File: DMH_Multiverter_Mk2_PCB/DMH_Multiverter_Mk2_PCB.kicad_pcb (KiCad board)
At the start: 2 copper layers, 32 x 75 mm, 24 parts, among them J0 Conn_01x01, J100 IDC_02x05, J200 BackBone_Connector_6pin, J50 Conn_01x06, J60 Conn_01x06, U1 TL072

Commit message: Main PCB update ongoing
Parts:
- added R6: 1k, Resistor_THT:R_Axial_DIN0207_L6.3mm_D2.5mm_P7.62mm_Horizontal, F.Cu at (152.5, 66.3)
- added R7: 10k, Resistor_THT:R_Axial_DIN0207_L6.3mm_D2.5mm_P7.62mm_Horizontal, F.Cu at (139.7, 53.4)
- added RV5: 50k, Potentiometer_THT:Potentiometer_Bourns_3296W_Vertical, F.Cu at (159.1, 54.6)
- added RV6: 50k, Potentiometer_THT:Potentiometer_Bourns_3296W_Vertical, F.Cu at (159.1, 61.0)
- C5, C6, D3, R1, R2, R3, R4, RV4: moved to F.Cu
- J50, J60: value Conn_01x06 -> Conn_01x08; moved to F.Cu
- R5: value 10k -> 33k; moved to F.Cu
- RV3: value 50k -> 100k; footprint Potentiometer_THT:Potentiometer_Bourns_3296W_Vertical -> SynthStuff:Potentiometer_TT_P110KH1; moved to F.Cu
- U1: value TL072 -> TL074; moved to F.Cu
- moved C5 104.6 mm to (148.2, 150.1)
- moved J50 100.1 mm to (149.0, 131.3), turned to 0 degrees
- moved C6 97.4 mm to (148.2, 153.5)
- moved D3 89.6 mm to (157.4, 130.8), turned to 0 degrees
- moved U1 82.7 mm to (118.3, 151.1), turned to 0 degrees
- moved R2 81.6 mm to (135.1, 141.6), turned to 0 degrees
- moved RV3 76.1 mm to (122.4, 147.3), turned to 0 degrees
- moved R4 74.7 mm to (135.1, 149.7), turned to 0 degrees
- moved R5 73.7 mm to (135.1, 153.7), turned to 0 degrees
- moved R1 73.2 mm to (135.1, 137.5), turned to 0 degrees
- moved RV4 67.9 mm to (141.7, 132.2), turned to 0 degrees
- moved R3 66.9 mm to (135.1, 145.6), turned to 0 degrees
- moved J60 66.2 mm to (153.6, 131.3), turned to 0 degrees
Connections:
- J200 pad 5: Net-(J200-Pin_2) -> Net-(J200-Pin_5)
- J50 pad 5: GND -> /Core Circuit/Att C Input
- J50 pad 6: GND -> /Core Circuit/Att C Output
- J60 pad 5: GND -> Net-(D3-K)
- J60 pad 6: GND -> Net-(J200-Pin_5)
- R5 pad 1: Net-(D3-K) -> /Core Circuit/Att C Input
- R5 pad 2: +12V -> Net-(U1C--)
- RV3 pad 1: Net-(U1A--) -> GND
- RV3 pad 2: Net-(R2-Pad1) -> Net-(U1C-+)
- RV3 pad 3: Net-(R2-Pad1) -> /Core Circuit/Att C Input
- RV4 pad 1: Net-(U1B--) -> Net-(U1A--)
- RV4 pad 2: Net-(R4-Pad1) -> Net-(R2-Pad1)
- RV4 pad 3: Net-(R4-Pad1) -> Net-(R2-Pad1)
- U1 pad 4: -12V -> +12V
- U1 pad 8: +12V -> Net-(R6-Pad1)
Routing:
- net +12V: track 63.2 -> 0.00 mm
- net /Core Circuit/Att B Input: track 54.7 -> 0.00 mm
- net -12V: track 47.9 -> 0.00 mm
- net /Core Circuit/Att B Output: track 36.5 -> 0.00 mm
- net /Core Circuit/Att A Output: track 30.8 -> 0.00 mm
- net /Core Circuit/Att A Input: track 30.0 -> 0.00 mm
- net Net-(R4-Pad1): track 27.5 -> 0.00 mm
- net Net-(U1B-+): track 26.7 -> 0.00 mm
- net Net-(D3-K): track 22.7 -> 0.00 mm
- net Net-(U1B--): track 22.4 -> 0.00 mm
- net Net-(U1A--): track 19.8 -> 0.00 mm
- net Net-(J200-Pin_2): track 19.3 -> 0.00 mm
- net Net-(R2-Pad1): track 17.6 -> 0.00 mm
- net Net-(D1-A): track 16.3 -> 0.00 mm
- net Net-(J200-Pin_1): track 13.7 -> 0.00 mm
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- removed copper zone on B.Cu, net GND
- removed copper zone on F.Cu, net GND
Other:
- board size 32 x 75 mm -> 32 x 124.5 mm
- board text removed: "Mk2.0 - December 2024"

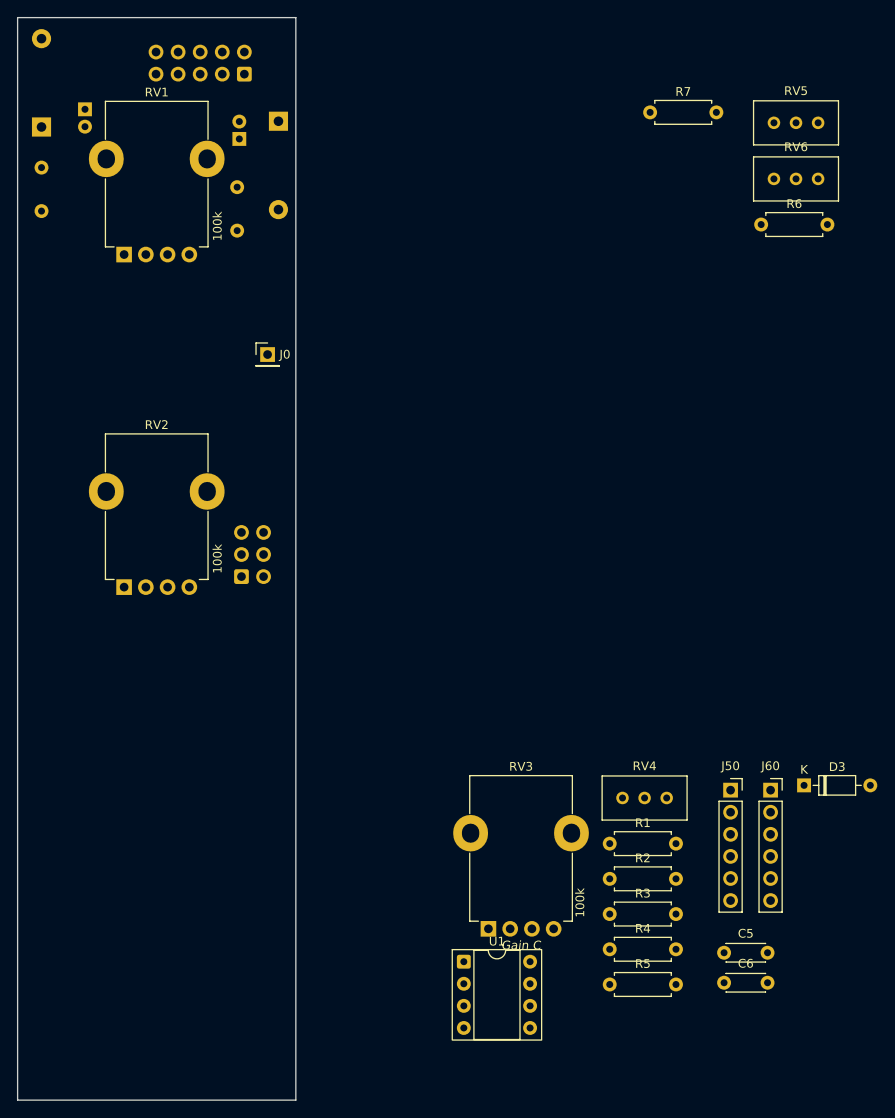
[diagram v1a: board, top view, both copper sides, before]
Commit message: Main PCB components placed
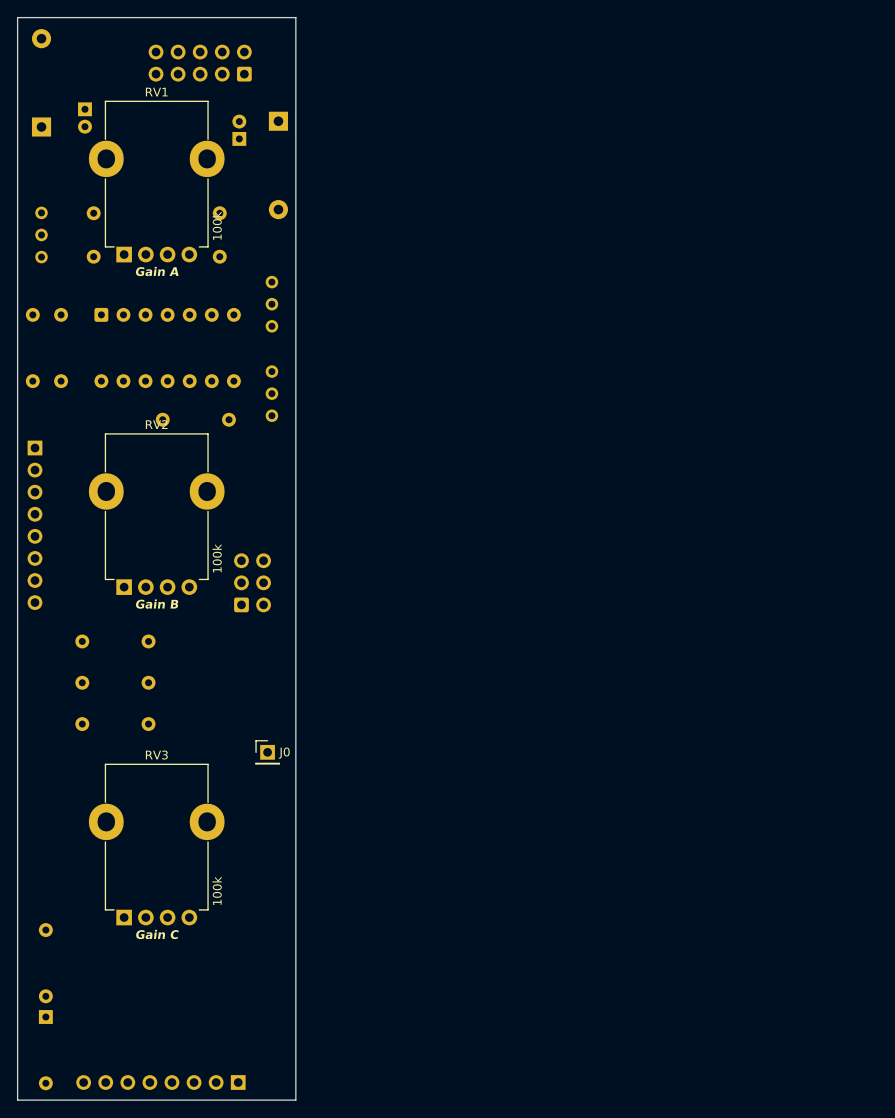
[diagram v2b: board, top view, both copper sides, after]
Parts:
- removed C5, C6: 100nF, Capacitor_THT:C_Disc_D4.3mm_W1.9mm_P5.00mm
- D3, R1, R2, R3, R4, R5, R6, R7, RV4, RV5, RV6: moved to B.Cu
- J50, J60: footprint Connector_PinSocket_2.54mm:PinSocket_1x06_P2.54mm_Vertical -> Connector_PinSocket_2.54mm:PinSocket_1x08_P2.54mm_Vertical; moved to B.Cu
- U1: footprint Package_DIP:DIP-8_W7.62mm_Socket -> Package_DIP:DIP-14_W7.62mm_Socket; moved to B.Cu
- moved R7 123.1 mm to (70.2, 155.1), turned to 90 degrees
- moved RV4 98.5 mm to (69.8, 65.0), turned to 90 degrees
- moved D3 91.2 mm to (70.2, 157.4), turned to -90 degrees
- moved R2 90.5 mm to (72.0, 76.7), turned to -90 degrees
- moved J50 89.2 mm to (69.0, 92.0), turned to 180 degrees
- moved U1 85.3 mm to (76.6, 76.7), turned to -90 degrees
- moved R1 85.0 mm to (68.8, 84.3), turned to 90 degrees
- moved J60 69.9 mm to (92.4, 165.0), turned to 90 degrees
- moved RV6 68.5 mm to (96.2, 88.3), turned to -90 degrees
- moved R5 67.7 mm to (74.4, 123.8)
- moved RV5 67.0 mm to (96.2, 78.0), turned to -90 degrees
- moved R6 65.2 mm to (91.3, 88.8), turned to 180 degrees
- moved R3 61.6 mm to (82.1, 114.2), turned to 180 degrees
- moved R4 61.3 mm to (82.1, 119.0), turned to 180 degrees
- moved J0 45.8 mm to (95.8, 127.0)
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
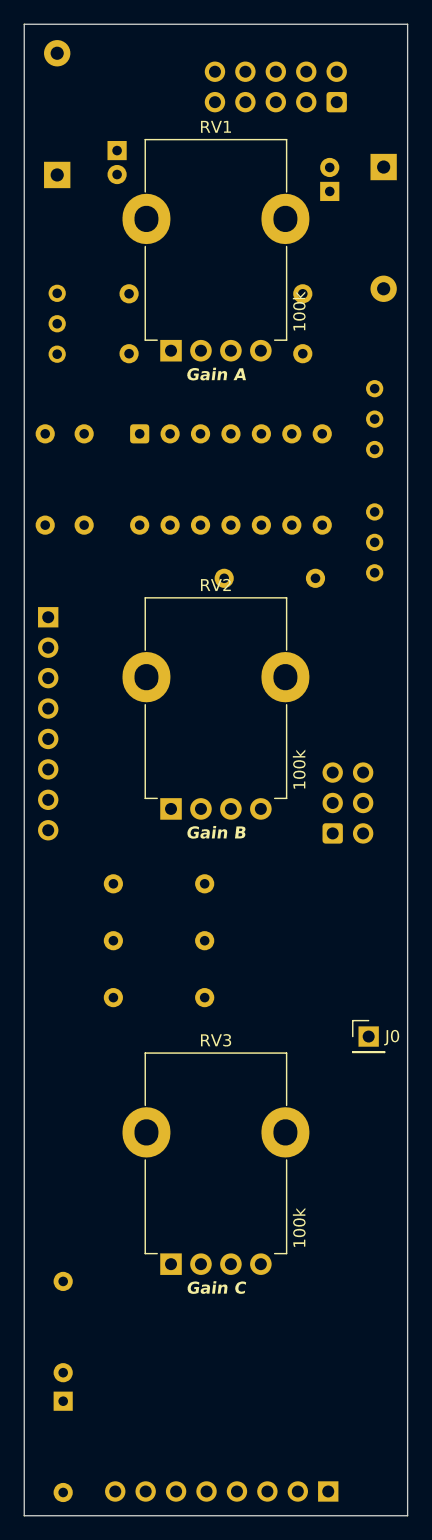
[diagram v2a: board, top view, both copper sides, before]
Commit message: Routed main PCB
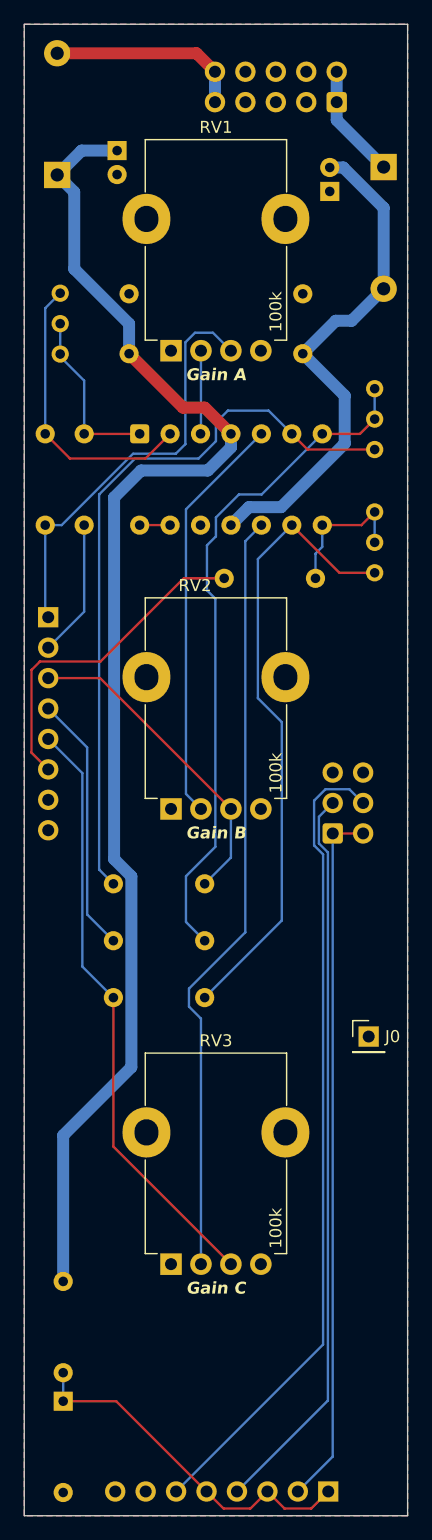
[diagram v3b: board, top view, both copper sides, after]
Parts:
- moved RV4 0.25 mm to (70.0, 65.0)
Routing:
- net +12V: track 0.00 -> 115.5 mm
- net Net-(J200-Pin_5): track 0.00 -> 68.0 mm
- net Net-(U1C-+): track 0.00 -> 64.6 mm
- net Net-(J200-Pin_2): track 0.00 -> 61.4 mm
- net Net-(U1B--): track 0.00 -> 61.1 mm
- net Net-(J200-Pin_1): track 0.00 -> 58.7 mm
- net Net-(R4-Pad1): track 0.00 -> 56.8 mm
- net Net-(U1C--): track 0.00 -> 52.7 mm
- net /Core Circuit/Att C Input: track 0.00 -> 50.2 mm
- net -12V: track 0.00 -> 42.9 mm
- net /Core Circuit/Att A Input: track 0.00 -> 35.5 mm
- net Net-(U1B-+): track 0.00 -> 34.4 mm
- net Net-(D3-K): track 0.00 -> 30.0 mm
- net /Core Circuit/Att C Output: track 0.00 -> 28.1 mm
- net /Core Circuit/Att B Input: track 0.00 -> 26.9 mm
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- added copper zone on B.Cu, net GND
- added copper zone on F.Cu, net GND
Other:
- board text added: "Mk2.0 - March 2025"

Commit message: Routed Connectors PCB
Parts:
- J50, J60: footprint Connector_PinSocket_2.54mm:PinSocket_1x08_P2.54mm_Vertical -> Connector_PinHeader_2.54mm:PinHeader_1x08_P2.54mm_Vertical
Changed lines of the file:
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@@
 	)
 	(footprint "Connector_PinHeader_2.54mm:PinHeader_1x01_P2.54mm_Vertical"
+		(locked yes)
 		(layer "F.Cu")
 		(at 95.75 127)
@@
 			(layer "B.Fab")
 		)
-		(fp_text user "${REFERENCE}"
-			(at -3.175 -0.005 90)
-			(layer "B.Fab")
-			(effects
-				(font
-					(size 1 1)
-					(thickness 0.15)
-				)
-				(justify mirror)
-			)
-		)
 		(pad "1" thru_hole circle
 			(at 0 0 90)
@@
 		)
 	)
-	(footprint "Connector_PinSocket_2.54mm:PinSocket_1x08_P2.54mm_Vertical"
+	(footprint "Connector_PinHeader_2.54mm:PinHeader_1x08_P2.54mm_Vertical"
+		(locked yes)
 		(layer "B.Cu")
 		(at 69 92 180)
-		(descr "Through hole straight socket strip, 1x08, 2.54mm pitch, single row (from Kicad 4.0.7), script generated")
-		(tags "Through hole socket strip THT 1x08 2.54mm single row")
+		(descr "Through hole straight pin header, 1x08, 2.54mm pitch, single row")
+		(tags "Through hole pin header THT 1x08 2.54mm single row")
 		(property "Reference" "J50"
-			(at 0 2.77 0)
+			(at 0 2.33 0)
 			(layer "B.SilkS")
 			(effects
@@
 		)
 		(property "Value" "Conn_01x08"
-			(at 0 -20.55 0)
+			(at 0 -20.11 0)
 			(layer "B.Fab")
 			(hide yes)
@@
 		(attr through_hole)
 		(fp_line
-			(start 1.33 1.33)
-			(end 1.33 0)
+			(start 1.33 -1.27)
+			(end 1.33 -19.11)
 			(stroke
 				(width 0.12)
@@
 		)
 		(fp_line
-			(start 1.33 -1.27)
-			(end 1.33 -19.11)
+			(start -1.33 1.33)
+			(end 0 1.33)
 			(stroke
 				(width 0.12)
@@
 		)
 		(fp_line
-			(start 0 1.33)
-			(end 1.33 1.33)
+			(start -1.33 0)
+			(end -1.33 1.33)
 			(stroke
 				(width 0.12)
@@
 		)
 		(fp_line
-			(start 1.75 1.8)
-			(end 1.75 -19.55)
+			(start 1.8 1.8)
+			(end -1.8 1.8)
 			(stroke
 				(width 0.05)
@@
 		)
 		(fp_line
-			(start 1.75 -19.55)
-			(end -1.8 -19.55)
+			(start 1.8 -19.55)
+			(end 1.8 1.8)
 			(stroke
 				(width 0.05)
@@
 		(fp_line
 			(start -1.8 1.8)
-			(end 1.75 1.8)
+			(end -1.8 -19.55)
 			(stroke
 				(width 0.05)
@@
 		(fp_line
 			(start -1.8 -19.55)
-			(end -1.8 1.8)
+			(end 1.8 -19.55)
 			(stroke
 				(width 0.05)
@@
 		)
 		(fp_line
-			(start 1.27 0.635)
+			(start 1.27 1.27)
 			(end 1.27 -19.05)
 			(stroke
@@
 		)
 		(fp_line
-			(start 0.635 1.27)
-			(end 1.27 0.635)
+			(start -0.635 1.27)
+			(end 1.27 1.27)
 			(stroke
 				(width 0.1)
@@
 		)
 		(fp_line
-			(start -1.27 1.27)
-			(end 0.635 1.27)
+			(start -1.27 0.635)
+			(end -0.635 1.27)
 			(stroke
 				(width 0.1)
@@
 		(fp_line
 			(start -1.27 -19.05)
-			(end -1.27 1.27)
+			(end -1.27 0.635)
 			(stroke
 				(width 0.1)
@@
 		)
 		(fp_text user "${REFERENCE}"
-			(at 0 -8.89 90)
+			(at 0 -8.89 270)
 			(layer "B.Fab")
 			(effects
@@
 		)
 		(embedded_fonts no)
-		(model "${KICAD9_3DMODEL_DIR}/Connector_PinSocket_2.54mm.3dshapes/PinSocket_1x08_P2.54mm_Vertical.wrl"
+		(model "${KICAD9_3DMODEL_DIR}/Connector_PinHeader_2.54mm.3dshapes/PinHeader_1x08_P2.54mm_Vertical.wrl"
 			(offset
 				(xyz 0 0 0)
@@
 		)
 	)
-	(footprint "Connector_PinSocket_2.54mm:PinSocket_1x08_P2.54mm_Vertical"
+	(footprint "Connector_PinHeader_2.54mm:PinHeader_1x08_P2.54mm_Vertical"
+		(locked yes)
 		(layer "B.Cu")
 		(at 92.375 164.975 90)
-		(descr "Through hole straight socket strip, 1x08, 2.54mm pitch, single row (from Kicad 4.0.7), script generated")
-		(tags "Through hole socket strip THT 1x08 2.54mm single row")
+		(descr "Through hole straight pin header, 1x08, 2.54mm pitch, single row")
+		(tags "Through hole pin header THT 1x08 2.54mm single row")
 		(property "Reference" "J60"
-			(at 0 2.77 90)
+			(at 0 2.33 270)
 			(layer "B.SilkS")
 			(effects
@@
 		)
 		(property "Value" "Conn_01x08"
-			(at 0 -20.55 90)
+			(at 0 -20.11 270)
 			(layer "B.Fab")
 			(hide yes)
@@
 		)
 		(fp_line
-			(start 1.33 1.33)
-			(end 1.33 0)
+			(start -1.33 0)
+			(end -1.33 1.33)
 			(stroke
 				(width 0.12)
@@
 		)
 		(fp_line
-			(start 0 1.33)
-			(end 1.33 1.33)
+			(start -1.33 1.33)
+			(end 0 1.33)
 			(stroke
 				(width 0.12)
@@
 		)
 		(fp_line
-			(start 1.75 -19.55)
-			(end -1.8 -19.55)
+			(start 1.8 -19.55)
+			(end 1.8 1.8)
 			(stroke
 				(width 0.05)
@@
 		(fp_line
 			(start -1.8 -19.55)
-			(end -1.8 1.8)
+			(end 1.8 -19.55)
 			(stroke
 				(width 0.05)
@@
 		)
 		(fp_line
-			(start 1.75 1.8)
-			(end 1.75 -19.55)
+			(start 1.8 1.8)
+			(end -1.8 1.8)
 			(stroke
 				(width 0.05)
@@
 		(fp_line
 			(start -1.8 1.8)
-			(end 1.75 1.8)
+			(end -1.8 -19.55)
 			(stroke
 				(width 0.05)
@@
 		(fp_line
 			(start -1.27 -19.05)
-			(end -1.27 1.27)
+			(end -1.27 0.635)
 			(stroke
 				(width 0.1)
@@
 		)
 		(fp_line
-			(start 1.27 0.635)
-			(end 1.27 -19.05)
+			(start -1.27 0.635)
+			(end -0.635 1.27)
 			(stroke
 				(width 0.1)
@@
 		)
 		(fp_line
-			(start 0.635 1.27)
-			(end 1.27 0.635)
+			(start 1.27 1.27)
+			(end 1.27 -19.05)
 			(stroke
 				(width 0.1)
@@
 		)
 		(fp_line
-			(start -1.27 1.27)
-			(end 0.635 1.27)
+			(start -0.635 1.27)
+			(end 1.27 1.27)
 			(stroke
 				(width 0.1)
@@
 		)
 		(fp_text user "${REFERENCE}"
-			(at 0 -8.89 0)
+			(at 0 -8.89 180)
 			(layer "B.Fab")
 			(effects
@@
 		)
 		(embedded_fonts no)
-		(model "${KICAD9_3DMODEL_DIR}/Connector_PinSocket_2.54mm.3dshapes/PinSocket_1x08_P2.54mm_Vertical.wrl"
+		(model "${KICAD9_3DMODEL_DIR}/Connector_PinHeader_2.54mm.3dshapes/PinHeader_1x08_P2.54mm_Vertical.wrl"
 			(offset
 				(xyz 0 0 0)

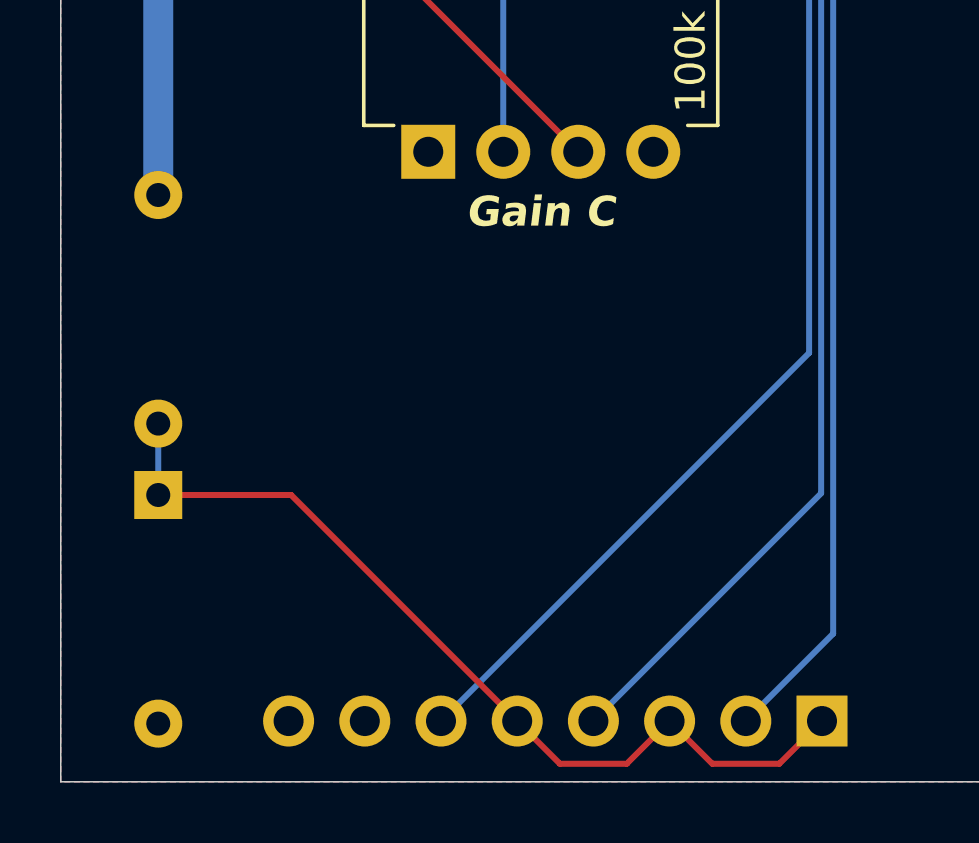
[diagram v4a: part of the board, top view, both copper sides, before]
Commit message: Independent zeners for normalled 5V DC offset
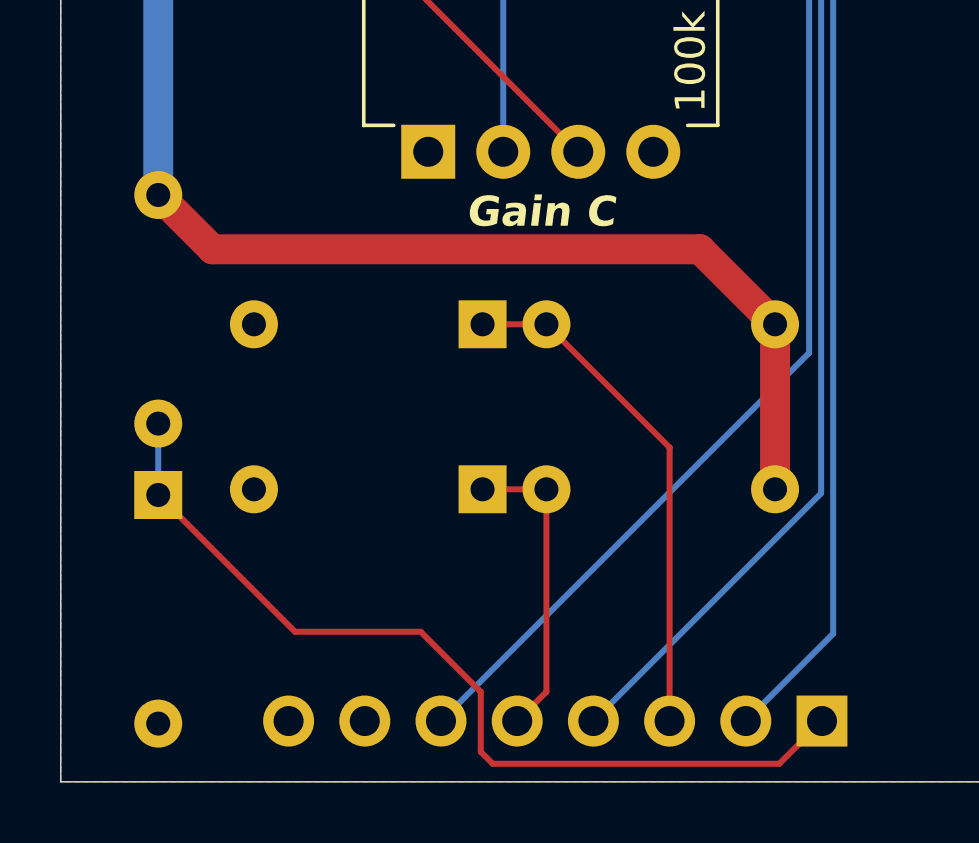
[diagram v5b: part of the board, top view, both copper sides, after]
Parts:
- added D4: ZPD5V1, Diode_THT:D_DO-35_SOD27_P7.62mm_Horizontal, B.Cu at (81.1, 151.8)
- added D5: ZPD5V1, Diode_THT:D_DO-35_SOD27_P7.62mm_Horizontal, B.Cu at (81.1, 157.2)
- added R8: 4k7, Resistor_THT:R_Axial_DIN0207_L6.3mm_D2.5mm_P7.62mm_Horizontal, B.Cu at (83.2, 151.8)
- added R9: 4k7, Resistor_THT:R_Axial_DIN0207_L6.3mm_D2.5mm_P7.62mm_Horizontal, B.Cu at (83.2, 157.2)
- R7: value 10k -> 4k7
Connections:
- J60 pad 3: Net-(D3-K) -> Net-(D4-K)
- J60 pad 5: Net-(D3-K) -> Net-(D5-K)
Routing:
- net +12V: track 115.5 -> 143.4 mm
- net Net-(D4-K): track 0.00 -> 17.1 mm
- net Net-(D5-K): track 0.00 -> 10.3 mm
